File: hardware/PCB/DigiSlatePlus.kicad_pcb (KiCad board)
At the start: 2 copper layers, 270 x 140 mm, 150 parts, among them J1 Serial, J10 IO7, J2 USB_B, J3 +8-24 Volt, J4 Battery, J6 Mains, J7 Timecode IN, J8 Timecode OUT, J9 MISO, Q1 2N2222, Q2 2N2222, Q3 FS8205A, Q4 2N2222, SW1 RotaryEncoder-SW, SW2 1, SW3 1, SW4 1, SW5 1, SW6 BOOT, SW7 SW_DPDT_x2, U1 ESP32-S3-WROOM-1, U10 MAX7219, U12 SA15-11SRWA, U13 SA15-11SRWA, U14 SA15-11SRWA, U15 SA15-11SRWA, U16 MAX7219, U17 SA15-11SRWA, U18 SA15-11SRWA, U19 SA15-11SRWA, U2 DS3231M, U20 SA15-11SRWA, U21 LM2596S-ADJ, U22 DW01A, U23 TP4056, U24 KA78M05_TO252, U25 LD1117S33TR_SOT223, U27 MAX7219, U29 MAX7219, U3 MAX7219, U31 MAX7219, U4 MAX7219, U6 MAX7219, U7 MAX7219

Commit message: new harware bugfixes while building the prototype
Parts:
- added C36: 10nF/50V, Capacitor_SMD:C_1206_3216Metric_Pad1.33x1.80mm_HandSolder, F.Cu at (248.5, 187.4)
- added C37: 100uF/10V, Capacitor_Tantalum_SMD:CP_EIA-7343-31_Kemet-D_Pad2.25x2.55mm_HandSolder, F.Cu at (253.8, 187.3)
- added C38: 10nF/50V, Capacitor_SMD:C_1206_3216Metric_Pad1.33x1.80mm_HandSolder, F.Cu at (253.5, 179.3)
- added C39: 10nF/50V, Capacitor_SMD:C_0805_2012Metric_Pad1.18x1.45mm_HandSolder, F.Cu at (249.2, 179.8)
- added C40: 100nF/50V, Capacitor_SMD:C_1206_3216Metric_Pad1.33x1.80mm_HandSolder, B.Cu at (334.0, 149.0)
- added D15: SS310, Diode_SMD:D_SMA, F.Cu at (260.2, 178.8)
- added L2: 68uH, Inductor_SMD:L_7.3x7.3_H3.5, F.Cu at (269.0, 187.7)
- added R35: 15k, Resistor_SMD:R_0805_2012Metric_Pad1.20x1.40mm_HandSolder, F.Cu at (258.8, 184.6)
- added R36: 15k, Resistor_SMD:R_0805_2012Metric_Pad1.20x1.40mm_HandSolder, F.Cu at (262.0, 184.6)
- added U33: MT3608, Package_TO_SOT_SMD:SOT-23-6, F.Cu at (260.4, 190.0)
- R24: value 180 -> 220
- R25: value 180 -> 120
- R31: value 100 -> 10k
- U23: footprint TP4056:TP4056-42-ESOP8_TPW -> TP4056:TP4056-42-SOP8_TPW_1
- moved R22 2.04 mm to (248.0, 174.8)
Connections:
- C13 pad 1: VCC-INT -> +6V
- C14 pad 1: VCC-INT -> +6V
- C17 pad 1: VCC-INT -> +6V
- C18 pad 1: VCC-INT -> +6V
- R1 pad 2: RST -> Net-(U1-EN)
- SW7 pad 3: VCC-INT -> SWITCHED
- U1 pad 3: RST -> Net-(U1-EN)
- U2 pad 16: SCL -> unconnected-(U2-SCL-Pad16)
- U24 pad 1: VCC-INT -> +6V
- U25 pad 3: VCC-INT -> +6V
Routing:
- net +6V: track 0.00 -> 79.8 mm, vias 0 -> 1
- net VCC-INT: track 72.0 -> 0.00 mm
- net RST: track 89.2 -> 40.3 mm
- net Net-(U1-EN): track 0.00 -> 47.2 mm
- net SWITCHED: track 0.00 -> 43.5 mm, vias 0 -> 2
- net Net-(U33-GND): track 0.00 -> 27.4 mm
- net Net-(D15-A): track 0.00 -> 16.6 mm
- net Net-(U33-FB): track 0.00 -> 7.61 mm
- net GND: track 507.5 -> 512.8 mm
- net Net-(U23-PROG): track 6.16 -> 4.18 mm
- net +BATT: track 45.3 -> 46.4 mm
- net CHARGER: track 121.6 -> 121.0 mm
- net Net-(U23-*STDBY): track 73.0 -> 72.4 mm
- net Net-(U23-*CHRG): track 74.6 -> 75.2 mm
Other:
- board text added: "3.3V"
- board text added: "GND"
- board text added: "RST"
- board text added: "RX"
- board text added: "TX"

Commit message: KiCAD bagfix update
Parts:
- J6: value Mains -> Slate
- R11: value 100 -> 1k5
- RV1: value 20K -> 10K
- moved J9 1.00 mm to (302.0, 117.5)
- moved C25 0.70 mm to (168.9, 136.1)
- moved C31 0.58 mm to (265.3, 136.1)
- moved C35 0.48 mm to (329.8, 136.1)
- moved C29 0.22 mm to (233.7, 136.1)
- moved C33 0.22 mm to (297.4, 136.1)
- moved C27 0.11 mm to (202.5, 136.1)
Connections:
- U2 pad 16: unconnected-(U2-SCL-Pad16) -> SCL
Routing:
- net MISO: track 28.3 -> 29.3 mm
- net +5V: track 782.3 -> 783.0 mm
- net Net-(U10-DIN): track 36.0 -> 36.7 mm
- net SCK: track 402.9 -> 403.5 mm
- net GND: track 512.8 -> 512.2 mm
- net Net-(C24-Pad2): track 30.7 -> 30.1 mm
- net D+: track 75.2 -> 75.7 mm
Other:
- board text added: "stdby"

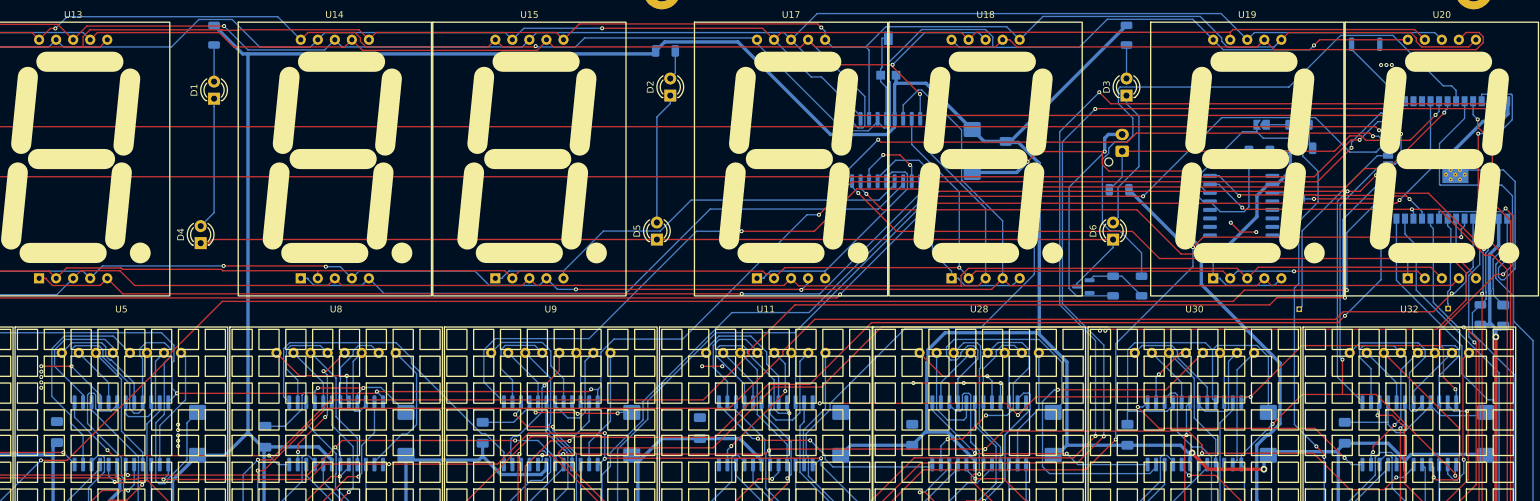
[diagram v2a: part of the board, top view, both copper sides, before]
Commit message: level converter added to schematic and pcb
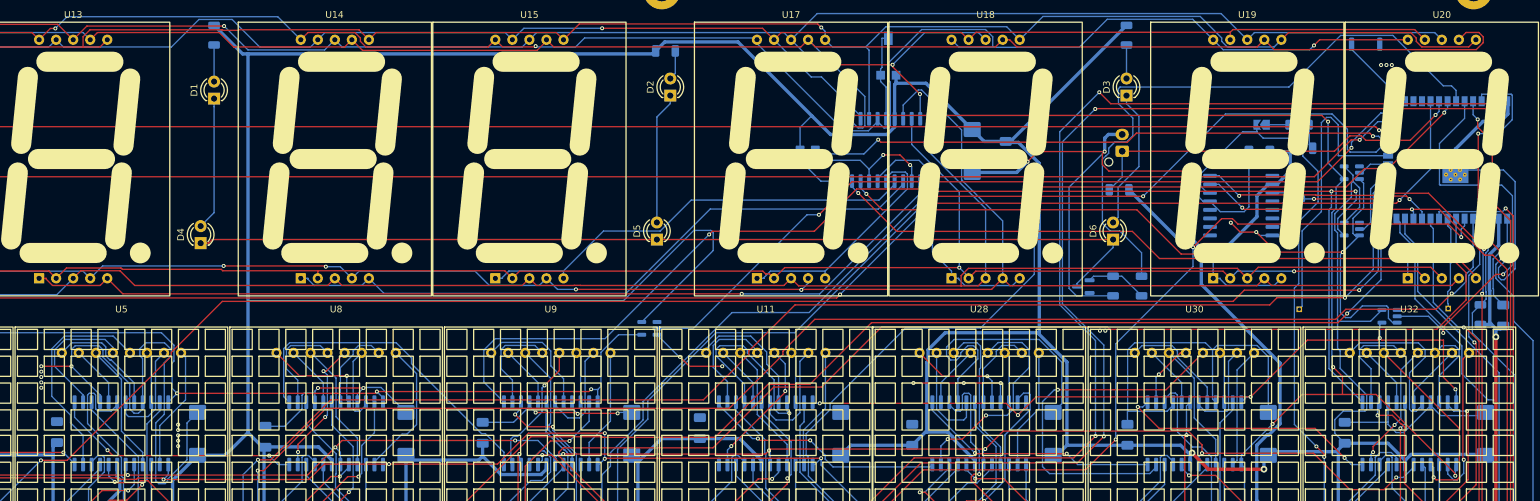
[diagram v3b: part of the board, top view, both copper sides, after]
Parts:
- added U34: SN74LV1T34DBV, Package_TO_SOT_SMD:SOT-23-5, B.Cu at (228.7, 94.3)
- added U35: SN74LV1T34DBV, Package_TO_SOT_SMD:SOT-23-5, B.Cu at (309.8, 97.2)
- added U36: SN74LV1T34DBV, Package_TO_SOT_SMD:SOT-23-5, B.Cu at (309.8, 105.5)
- added U37: SN74LV1T34DBV, Package_TO_SOT_SMD:SOT-23-5, B.Cu at (315.5, 118.5)
- added U38: SN74LV1T34DBV, Package_TO_SOT_SMD:SOT-23-5, B.Cu at (205.1, 120.3)
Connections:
- U10 pad 12: LOAD-1 -> LOAD1-5V
- U10 pad 13: SCK -> SCK-5V
- U16 pad 1: MOSI -> MOSI-5V
- U16 pad 12: LOAD-TC -> LOADTC-5V
- U16 pad 13: SCK -> SCK-5V
- U27 pad 12: LOAD-1 -> LOAD1-5V
- U27 pad 13: SCK -> SCK-5V
- U29 pad 12: LOAD-1 -> LOAD1-5V
- U29 pad 13: SCK -> SCK-5V
- U3 pad 12: LOAD-2 -> LOAD2-5V
- U3 pad 13: SCK -> SCK-5V
- U31 pad 1: MOSI -> MOSI-5V
- U31 pad 12: LOAD-1 -> LOAD1-5V
- U31 pad 13: SCK -> SCK-5V
- U4 pad 12: LOAD-2 -> LOAD2-5V
- U4 pad 13: SCK -> SCK-5V
- U6 pad 12: LOAD-2 -> LOAD2-5V
- U6 pad 13: SCK -> SCK-5V
- U7 pad 1: MOSI -> MOSI-5V
- U7 pad 12: LOAD-2 -> LOAD2-5V
- U7 pad 13: SCK -> SCK-5V
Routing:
- net SCK: track 403.5 -> 5.31 mm, vias 11 -> 0
- net SCK-5V: track 0.00 -> 390.9 mm, vias 0 -> 11
- net MOSI-5V: track 0.00 -> 192.4 mm, vias 0 -> 4
- net MOSI: track 190.2 -> 11.2 mm, vias 4 -> 0
- net +5V: track 783.0 -> 944.2 mm
- net LOAD-2: track 256.5 -> 122.7 mm, vias 5 -> 2
- net LOAD2-5V: track 0.00 -> 131.1 mm, vias 0 -> 3
- net LOAD1-5V: track 0.00 -> 116.3 mm, vias 0 -> 5
- net LOAD-1: track 165.2 -> 59.0 mm, vias 5 -> 2
- net GND: track 512.2 -> 580.4 mm, vias 72 -> 73
- net MISO: track 29.3 -> 44.5 mm
- net LOADTC-5V: track 0.00 -> 7.76 mm
- net RS: track 209.4 -> 211.7 mm
- net SW2: track 242.5 -> 244.7 mm
- net LOAD-TC: track 85.4 -> 87.3 mm
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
